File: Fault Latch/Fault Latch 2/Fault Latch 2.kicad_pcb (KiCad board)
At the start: 2 copper layers, 351.1 x 116.3 mm, 111 parts, among them K102 Fujitsu_FTR-LYAA005x, K103 Fujitsu_FTR-LYAA005x, K104 Fujitsu_FTR-LYAA005x, Q102 Q_NMOS_GSD, Q104 Q_NPN_BEC, Q105 Q_PMOS_GSD, Q106 Q_NPN_BEC, Q107 Q_NPN_BEC, Q108 Q_NPN_BEC, Q109 Q_PMOS_GSD, Q110 Q_PMOS_GSD, Q111 Q_NMOS_GDS, Q112 Q_NPN_BEC, Q113 Q_NPN_BEC, Q114 Q_NMOS_GDS, Q115 Q_NMOS_GSD, Q116 Q_NMOS_GSD, Q117 Q_NMOS_GDS, Q118 Q_PMOS_GSD, SW101 SW_Omron_B3FS, SW102 SW_Omron_B3FS, SW103 SW_Omron_B3FS, U101 641964-1, U102 74AHC1G00, U103 74AHC1G00, U104 74AHC1G00, U105 641964-1, U106 74LS279, U111 641964-1, U112 641964-1, U113 641964-1, U114 SFH617A-1, U115 SFH617A-1, U116 SFH617A-1, U117 641964-1, U118 LM555xM, U119 641964-1, U120 74AHC1G08, U121 641964-1, U122 641964-1, U125 SFH617A-1, U126 SFH617A-1, U127 SFH617A-1

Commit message: Fault Latch V2.0 waiting for final check
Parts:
- removed D1, D2, D3, D4: US2AA, Diode_SMD:D_SMA
- added D110: D_Schottky, Diode_SMD:D_SMA, F.Cu at (125.6, 109.3)
- added D111: D_Schottky, Diode_SMD:D_SMA, F.Cu at (121.0, 109.3)
- added D112: D_Schottky, Diode_SMD:D_SMA, F.Cu at (85.0, 135.0)
- added D113: D_Schottky, Diode_SMD:D_SMA, F.Cu at (85.0, 144.5)
- added Q103: Q_NMOS_GSD, Package_TO_SOT_SMD:SOT-23, F.Cu at (122.8, 133.1)
- added R117: 500R, Resistor_SMD:R_0603_1608Metric, F.Cu at (125.3, 137.5)
- moved H104 31.3 mm to (77.2, 43.0)
- moved H101 29.7 mm to (76.8, 145.5)
- moved H103 20.9 mm to (157.5, 43.5)
- moved H102 17.8 mm to (157.2, 145.0)
- moved Q102 3.75 mm to (127.8, 135.8), turned to 90 degrees
- moved U101 0.85 mm to (139.2, 82.1)
- moved U105 0.85 mm to (139.2, 92.7)
- moved U121 0.31 mm to (139.2, 115.7)
- moved U119 0.26 mm to (139.2, 104.2)
- moved U117 0.15 mm to (138.6, 46.1)
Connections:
- Q102 pad 1: /IMD_LED -> Net-(Q102-G)
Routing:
- net Net-(Q102-D): track 37.0 -> 16.2 mm
- net GNDPWR: track 22.5 -> 2.84 mm, vias 0 -> 2
- net Net-(Q102-G): track 0.00 -> 8.05 mm
- net +12V: track 124.5 -> 126.2 mm, vias 5 -> 4
- net /IMD_LED: track 47.0 -> 45.7 mm
- net /BMS_SR: track 110.3 -> 109.1 mm
- net /IMD_HV: track 26.2 -> 27.1 mm
- net /BSPD_HV: vias 2 -> 0
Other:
- board size 351.1 x 116.3 mm -> 89.6 x 111.1 mm
- board text added: "FAULT LATCH V2.0"
- board text removed: "FAULT LATCH V1.0"

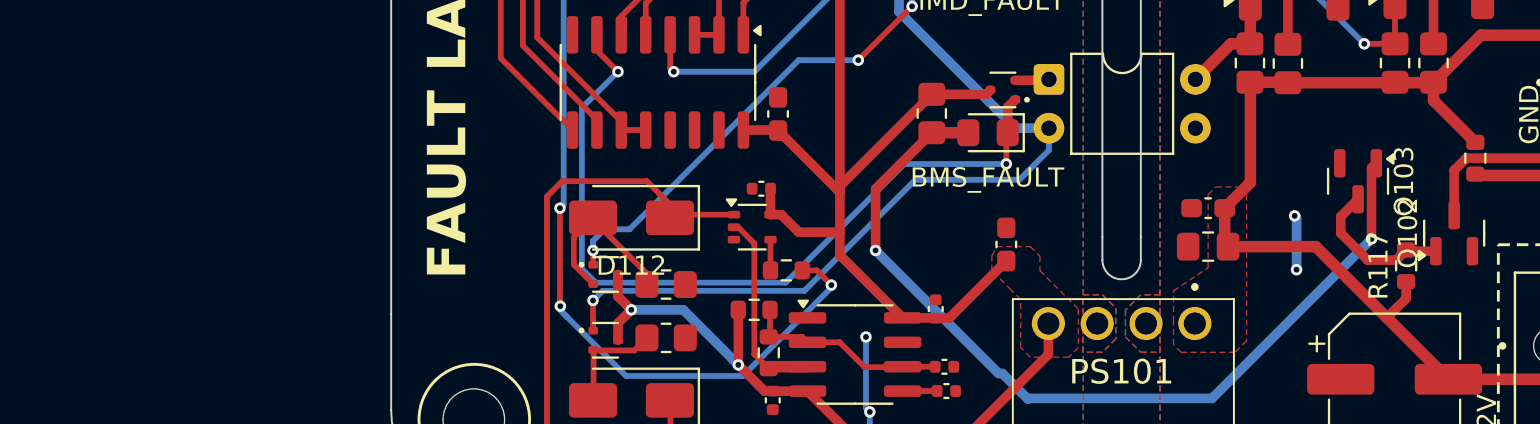
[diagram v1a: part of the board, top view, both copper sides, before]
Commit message: BSPD needs to be fixed + Fault Latch Layout Issue
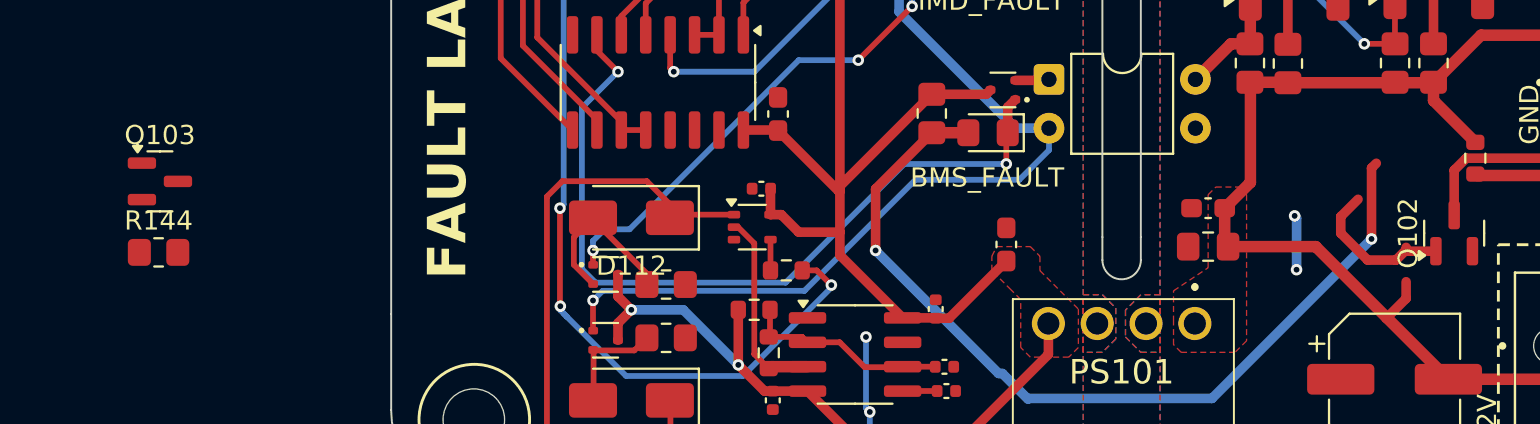
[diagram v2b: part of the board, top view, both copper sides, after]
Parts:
- removed R117: 500R, Resistor_SMD:R_0603_1608Metric
- added R144: 10k, Resistor_SMD:R_0805_2012Metric_Pad1.20x1.40mm_HandSolder, F.Cu at (60.4, 136.8)
- moved Q103 62.3 mm to (60.5, 133.1), turned to 0 degrees
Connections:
- D107 pad 2: /IMD_LED -> Net-(D107-A)
- Q105 pad 2: Net-(Q105-S) -> +5V
- Q105 pad 3: +5V -> Net-(Q105-D)
- Q109 pad 2: Net-(Q109-S) -> +5V
- Q109 pad 3: +5V -> Net-(Q109-D)
- Q110 pad 2: Net-(D112-A) -> +5V
- Q110 pad 3: +5V -> Net-(D112-A)
- Q114 pad 1: Net-(Q114-G) -> /IMD_LED
- Q118 pad 2: Net-(D113-A) -> +5V
- Q118 pad 3: +5V -> Net-(D113-A)
- R134 pad 1: /IMD_LED -> Net-(D107-A)
- R137 pad 2: Net-(Q114-G) -> /IMD_LED
- U125 pad 1: Net-(Q105-S) -> Net-(Q105-D)
- U125 pad 4: Net-(Q114-G) -> /IMD_LED
- U127 pad 1: Net-(Q109-S) -> Net-(Q109-D)
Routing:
- net Net-(D107-A): track 0.00 -> 45.7 mm, vias 0 -> 2
- net /IMD_LED: track 45.7 -> 5.91 mm, vias 2 -> 0
- net Net-(Q114-G): track 5.91 -> 0.00 mm
- net +5V: track 303.4 -> 306.9 mm
- net Net-(Q105-S): track 1.77 -> 0.00 mm
- net Net-(Q109-S): track 1.68 -> 0.00 mm

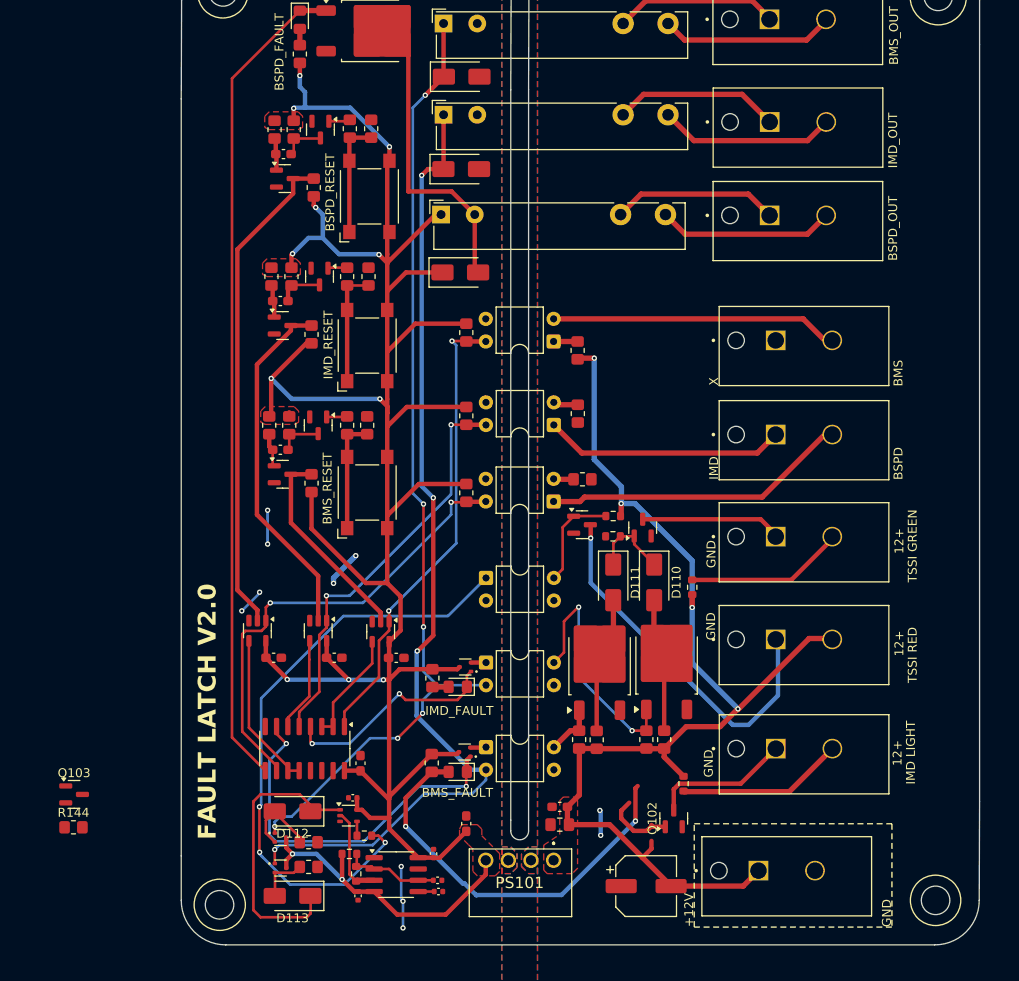
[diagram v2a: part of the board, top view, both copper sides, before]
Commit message: Fault latch added Logo
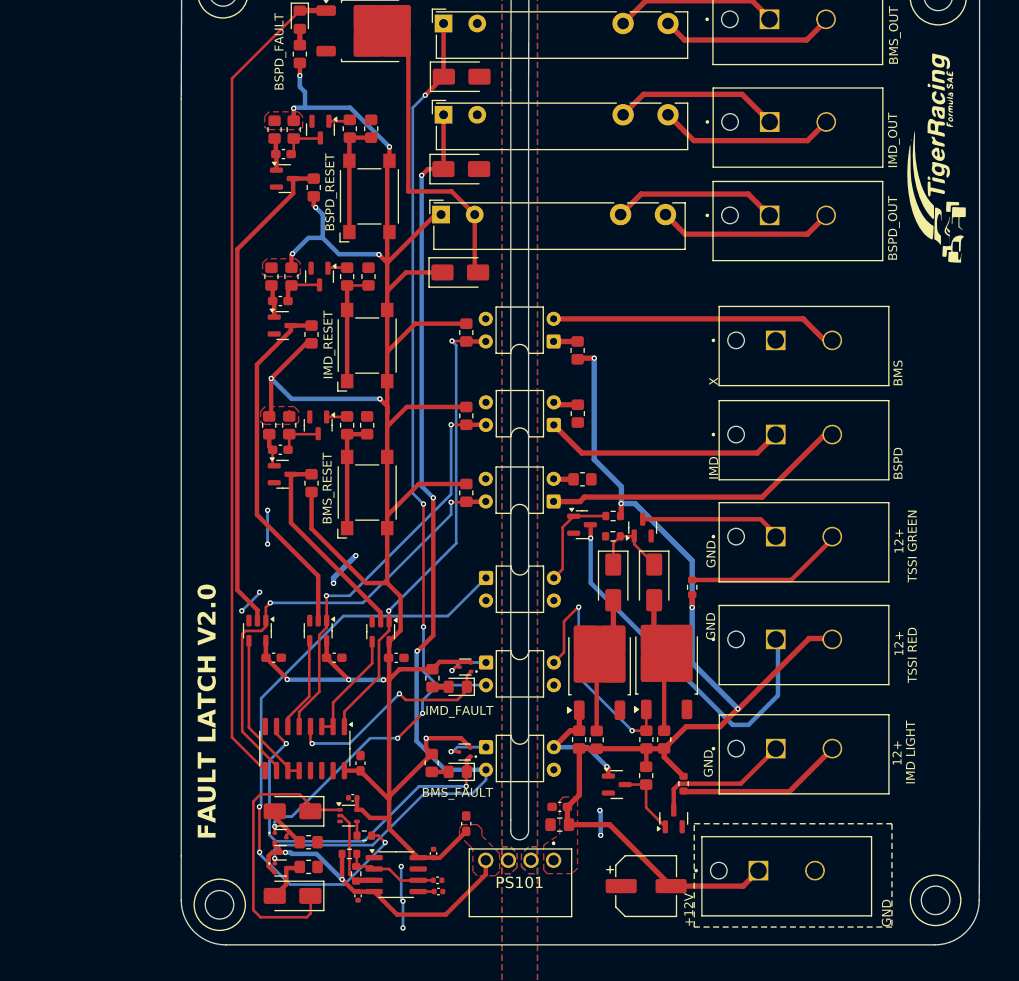
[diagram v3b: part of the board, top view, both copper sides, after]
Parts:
- added G***: LOGO, LOGO, F.Cu at (158.8, 69.9)
- added G***: LOGO, LOGO, F.Cu at (157.4, 61.7)
- moved R144 64.6 mm to (124.7, 131.0), turned to -90 degrees
- moved Q103 60.9 mm to (121.4, 132.0)
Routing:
- net Net-(D107-A): track 45.7 -> 1.90 mm, vias 2 -> 0
- net /IMD_LED: track 5.91 -> 13.9 mm, vias 0 -> 1
- net Net-(Q105-D): track 0.00 -> 5.21 mm, vias 0 -> 1
- net Net-(Q109-D): track 0.00 -> 5.21 mm, vias 0 -> 1
- net +5V: track 306.9 -> 311.8 mm, vias 13 -> 14
- net Net-(D112-A): track 8.79 -> 5.96 mm
- net /IMD_SR: track 110.8 -> 112.5 mm

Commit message: FAULT LATCH CHANGES
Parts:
- removed D112, D113: D_Schottky, Diode_SMD:D_SMA
- removed the Q110 at (83.7, 137.9)
- removed Q114, Q117: Q_NMOS_GDS, Package_TO_SOT_SMD:TO-252-2
- removed Q115: Q_NMOS_GSD, Package_TO_SOT_SMD:SOT-23
- removed Q118: Q_PMOS_GSD, Package_TO_SOT_SMD:SOT-523
- removed R139, R140, R141, R142: 10k, Resistor_SMD:R_0805_2012Metric_Pad1.20x1.40mm_HandSolder
- removed the U120 at (91.3, 135.5)
- added C112: 0.1u, Capacitor_SMD:C_0402_1005Metric, F.Cu at (65.4, 83.7)
- added Q113: Q_PMOS_GSD, Package_TO_SOT_SMD:SOT-523, F.Cu at (65.8, 81.1)
- added U117: 74AHC1G00, Package_TO_SOT_SMD:SOT-23-5, F.Cu at (61.4, 81.9)
- added U119: 74AHC1G00, Package_TO_SOT_SMD:SOT-23-5, F.Cu at (61.4, 86.5)
- renumbered C113 to C107, C114 to C108, C115 to C109, C117 to C110, C116 to C111, C107 to C113, C108 to C114, C109 to C115, C110 to C116, C111 to C117, D107 to D101, D103 to D102, D108 to D103, D109 to D104, D106 to D105, D105 to D106, D110 to D107, D111 to D108, K104 to K101, K103 to K102, K102 to K103, Q104 to Q101, Q106 to Q102, Q107 to Q103, Q108 to Q104, Q103 to Q105, Q102 to Q106, Q109 to Q107, Q105 to Q108, Q111 to Q109, Q112 to Q110, Q113 to Q111, Q116 to Q112, R129 to R102, R131 to R103, R135 to R104, R102 to R105, R107 to R106, R105 to R107, R106 to R108, R104 to R109, R108 to R110, R109 to R111, R116 to R112, R112 to R113, R113 to R114, R114 to R115, R134 to R116, R133 to R117, R136 to R118, R115 to R119, R144 to R121, R124 to R122, R125 to R123, R126 to R124, R138 to R125, R137 to R126, R123 to R128, R128 to R129, R122 to R130, R111 to R131, R130 to R132, R132 to R133, R143 to R134, U114 to U101, U115 to U102, U116 to U103, U102 to U104, U103 to U105, U104 to U106, U106 to U107, U122 to U108, U127 to U109, U125 to U110, U117 to U111, U111 to U112, U112 to U113, U119 to U114, U101 to U115, U105 to U116, U113 to U120, U126 to U121, U121 to U122
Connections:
- C110 pad 1: +5V -> GND
- C110 pad 2: GND -> +5V
- D101 pad 1: Net-(D107-K) (its old number) -> /IMD_SR
- D102 pad 1: Net-(D103-K) (its old number) -> /BMS_SR
- D104 pad 1: /BMS_SR -> Net-(D104-K)
- D106 pad 1: /IMD_SR -> Net-(D106-K)
- D108 pad 2: /IMD_Green -> /IMD_LED
- K101 pad A1: /BMS_SR -> Net-(D104-K)
- K103 pad A1: /IMD_SR -> Net-(D106-K)
- Q107 pad 1: Net-(D103-K) (its old number) -> /BMS_SR
- Q108 pad 1: Net-(D107-K) (its old number) -> /IMD_SR
- R125 pad 2: Net-(Q117-G) -> /BMS_Green
- R133 pad 1: Net-(R132-Pad1) -> Net-(R133-Pad1)
- R133 pad 2: Net-(R132-Pad2) -> Net-(R133-Pad2)
- U107 pad 4: Net-(D103-K) (its old number) -> /BMS_SR
- U107 pad 7: Net-(D107-K) (its old number) -> /IMD_SR
- U109 pad 2: /BMS_SR -> Net-(D104-K)
- U109 pad 4: Net-(Q117-G) -> /BMS_Green
- U110 pad 2: /IMD_SR -> Net-(D106-K)
- U121 pad 1: Net-(R132-Pad2) -> +5V
- U121 pad 2: GND -> Net-(R133-Pad1)
- U122 pad 1: Net-(Q115-D) -> GNDPWR
- U122 pad 2: +12V -> Net-(Q113-D)
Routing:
- net Net-(D106-K): track 0.00 -> 112.5 mm, vias 0 -> 4
- net Net-(D104-K): track 0.00 -> 109.1 mm, vias 0 -> 6
- net /BMS_SR: track 109.1 -> 24.7 mm, vias 6 -> 2
- net /IMD_SR: track 112.5 -> 41.9 mm, vias 4 -> 2
- net Net-(R132-Pad2): track 68.1 -> 0.00 mm, vias 3 -> 0
- net +5V: track 311.8 -> 379.8 mm, vias 14 -> 17
- net (no net): track 0.00 -> 51.2 mm
- net Net-(Q115-D): track 42.1 -> 0.00 mm, vias 1 -> 0
- net GNDPWR: track 2.84 -> 45.0 mm, vias 2 -> 3
- net Net-(D107-K) (its old number): track 41.9 -> 0.00 mm, vias 2 -> 0
- net Net-(D112-K): track 32.6 -> 0.00 mm
- net Net-(Q117-G): track 27.8 -> 0.00 mm, vias 2 -> 0
- net /BMS_Green: track 11.9 -> 39.7 mm, vias 0 -> 2
- net Net-(D103-K) (its old number): track 24.7 -> 0.00 mm, vias 2 -> 0
- net /IMD_Green: track 11.9 -> 0.00 mm
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
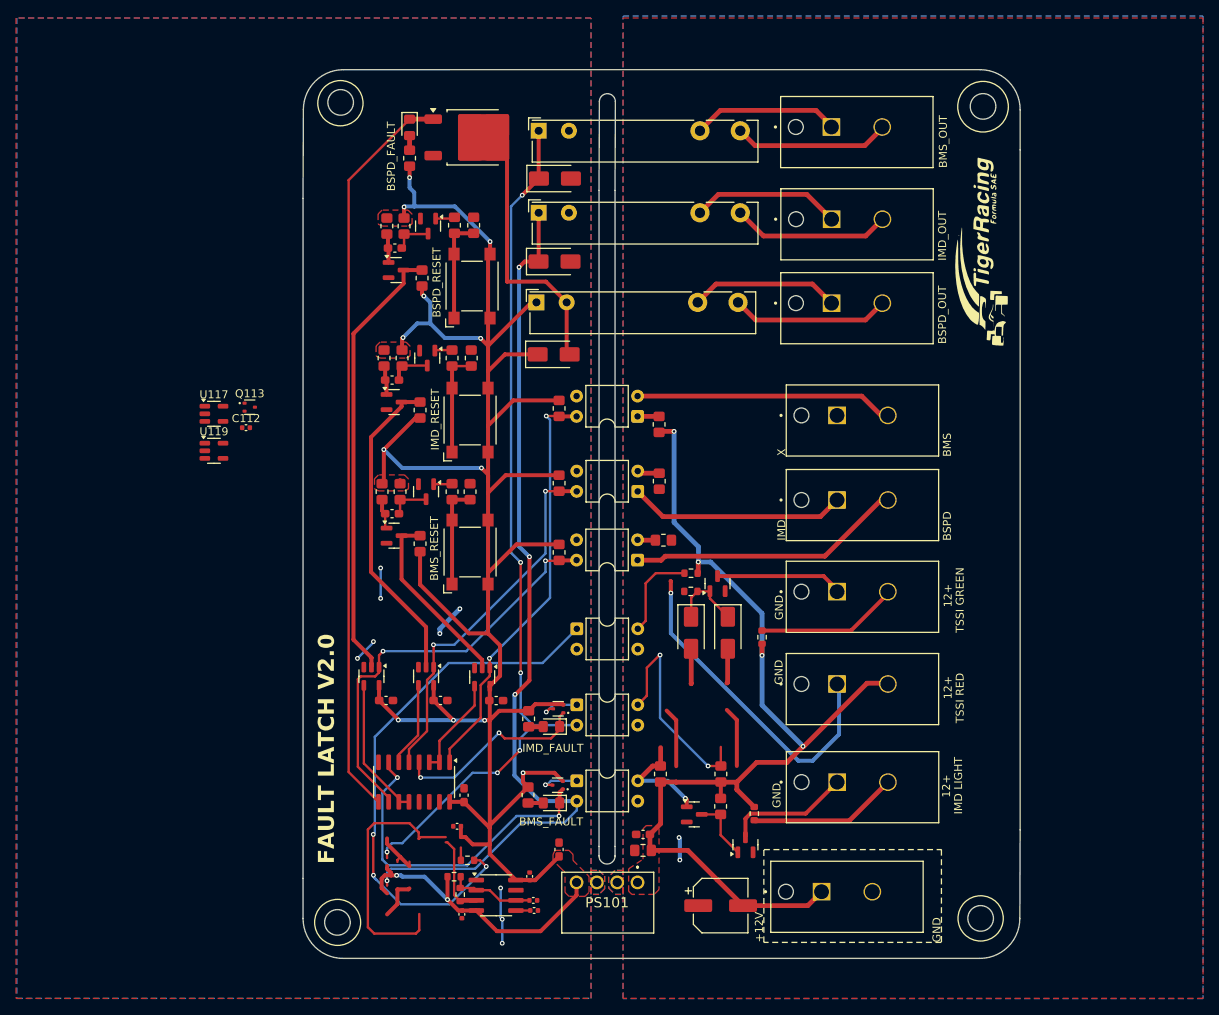
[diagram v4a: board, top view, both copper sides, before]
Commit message: Fixed Fault Latch Layout
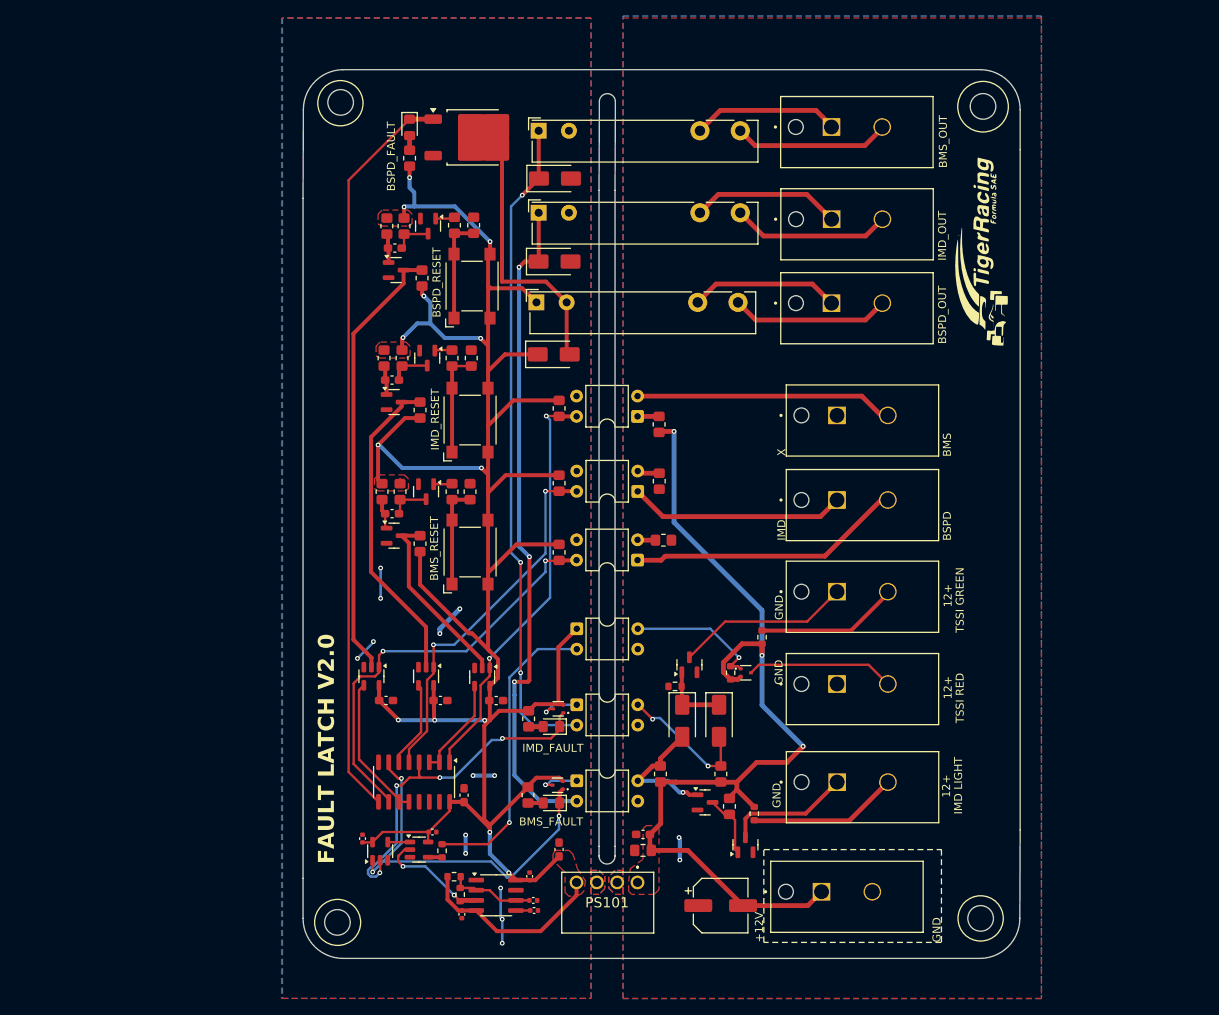
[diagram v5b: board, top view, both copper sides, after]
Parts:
- moved Q113 70.3 mm to (127.8, 114.3)
- moved U117 58.5 mm to (82.1, 136.6), turned to 90 degrees
- moved U119 56.1 mm to (87.0, 136.4)
- moved C112 55.7 mm to (88.7, 134.2), turned to 180 degrees
- moved R134 13.4 mm to (125.9, 114.3), turned to 90 degrees
- moved R128 12.0 mm to (119.0, 116.0)
- moved C110 11.9 mm to (79.9, 135.0), turned to -90 degrees
- moved D107 11.1 mm to (124.5, 120.3)
- moved D108 11.1 mm to (119.9, 120.3)
- moved Q112 10.7 mm to (120.8, 113.3)
- moved R133 3.40 mm to (89.9, 136.6), turned to -90 degrees
- moved Q105 2.02 mm to (122.8, 130.5)
- moved R121 1.10 mm to (125.8, 131.0)
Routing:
- net +5V: track 379.8 -> 317.5 mm, vias 17 -> 13
- net (no net): track 51.2 -> 0.00 mm
- net GNDPWR: track 45.0 -> 3.25 mm, vias 3 -> 2
- net Net-(R133-Pad1): track 1.60 -> 37.6 mm, vias 0 -> 1
- net Net-(D106-K): track 112.5 -> 83.8 mm, vias 4 -> 3
- net Net-(D104-K): track 109.1 -> 82.4 mm, vias 6 -> 3
- net /BMS_Green: track 39.7 -> 17.4 mm
- net /BMS_SR: track 24.7 -> 43.8 mm, vias 2 -> 4
- net Net-(Q113-D): track 0.00 -> 18.7 mm
- net +12V: track 125.9 -> 118.6 mm, vias 4 -> 3
- net /IMD_SR: track 41.9 -> 48.2 mm, vias 2 -> 3
- net Net-(Q112-D): track 16.0 -> 21.8 mm
- net Net-(Q113-G): track 11.4 -> 17.1 mm, vias 0 -> 1
- net GND: track 17.8 -> 22.9 mm, vias 9 -> 13
- net /CLOCK: track 10.3 -> 14.3 mm, vias 0 -> 2
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
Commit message: FL READY
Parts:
- added G***: LOGO, LOGO, F.Cu at (128.3, 97.3)
- moved H104 97.2 mm to (174.2, 49.1), turned to -90 degrees
- moved H101 96.5 mm to (74.2, 49.1), turned to -90 degrees
- moved D103 88.6 mm to (173.6, 58.1), turned to 180 degrees
- moved H103 87.2 mm to (174.2, 129.1), turned to -90 degrees
- moved H102 84.5 mm to (74.2, 129.1), turned to -90 degrees
- moved R118 84.3 mm to (169.7, 58.1), turned to 180 degrees
- moved C110 82.9 mm to (84.7, 52.2), turned to 180 degrees
- moved U117 82.2 mm to (83.1, 54.4), turned to 0 degrees
- moved C108 81.7 mm to (75.2, 64.6), turned to 180 degrees
- moved Q109 80.7 mm to (172.3, 66.1), turned to -90 degrees
- moved R131 78.9 mm to (77.7, 64.4), turned to 0 degrees
- moved R127 78.4 mm to (161.3, 55.2), turned to 180 degrees
- moved U119 77.2 mm to (83.3, 59.3), turned to -90 degrees
- moved R132 77.0 mm to (79.9, 63.7), turned to 90 degrees
- moved K101 76.4 mm to (173.2, 74.2), turned to -90 degrees
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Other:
- board size 89.6 x 111.1 mm -> 110 x 90 mm
